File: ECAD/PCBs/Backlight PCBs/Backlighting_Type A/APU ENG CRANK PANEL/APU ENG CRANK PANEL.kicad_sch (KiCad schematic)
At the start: 46 parts, among them J1 Molex 2x02 Mini-Fit Jr., J2 Molex 2x02 Mini-Fit Jr.

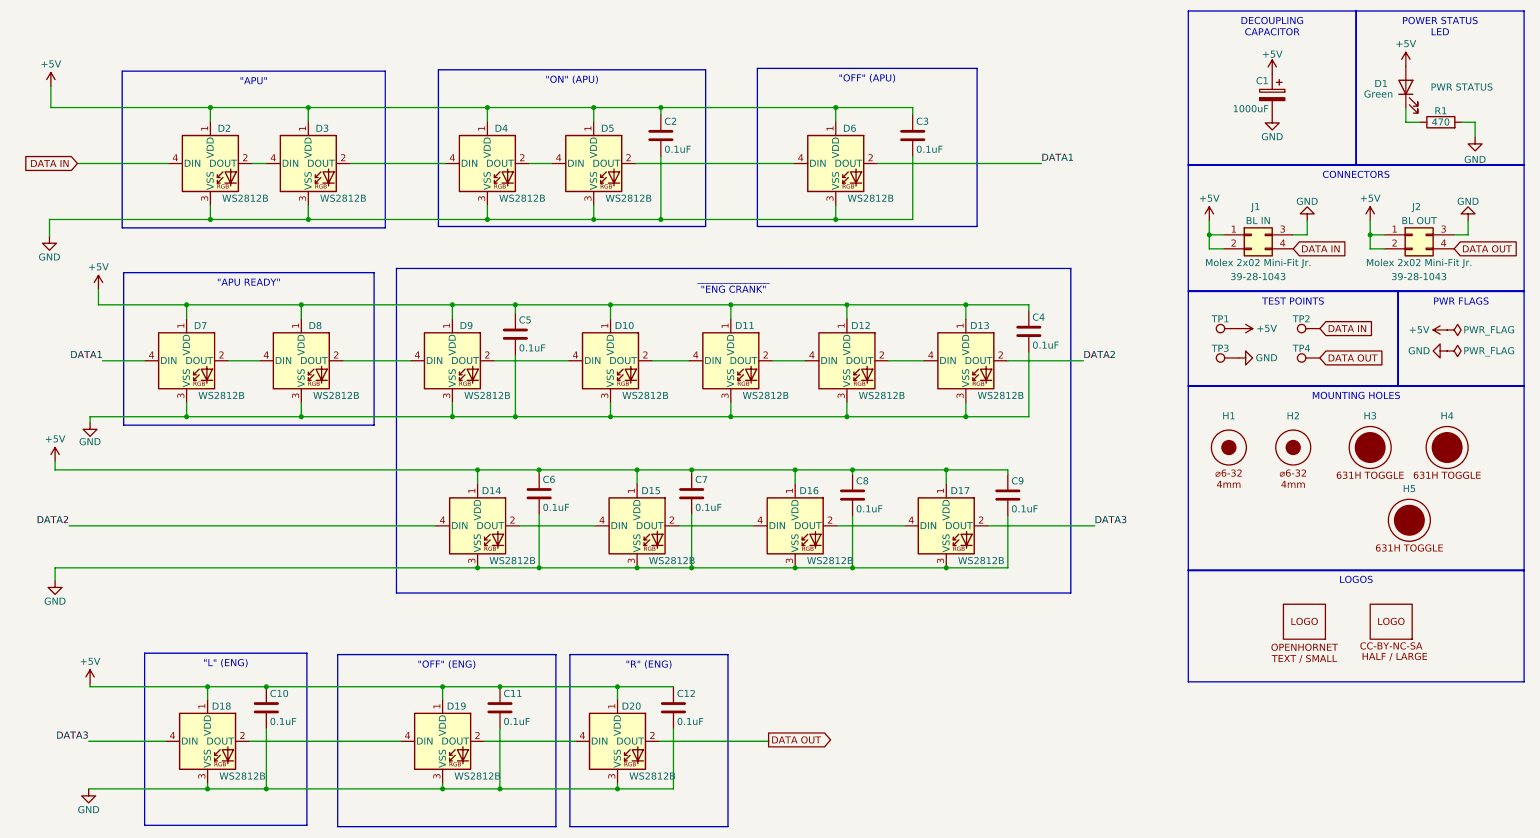
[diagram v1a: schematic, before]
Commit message: Updated schematics:  ANT SEL & APU ENG panels
1:  Updated Schematic/PCB Netlists from default to 5v/GND as required.
2:  Reannotated Test Point references designators.  To prevent confusion, TP1 & 2 will also be Power/Ground respectively; TP3 and TP4 will be Data In/Data Out respectively.
3:  Updated schematic/pcb with symbol/footprint metadata
4:  Fixed "DATA OUT" symbols on TestPoint and J2 connector to show output instead of input.
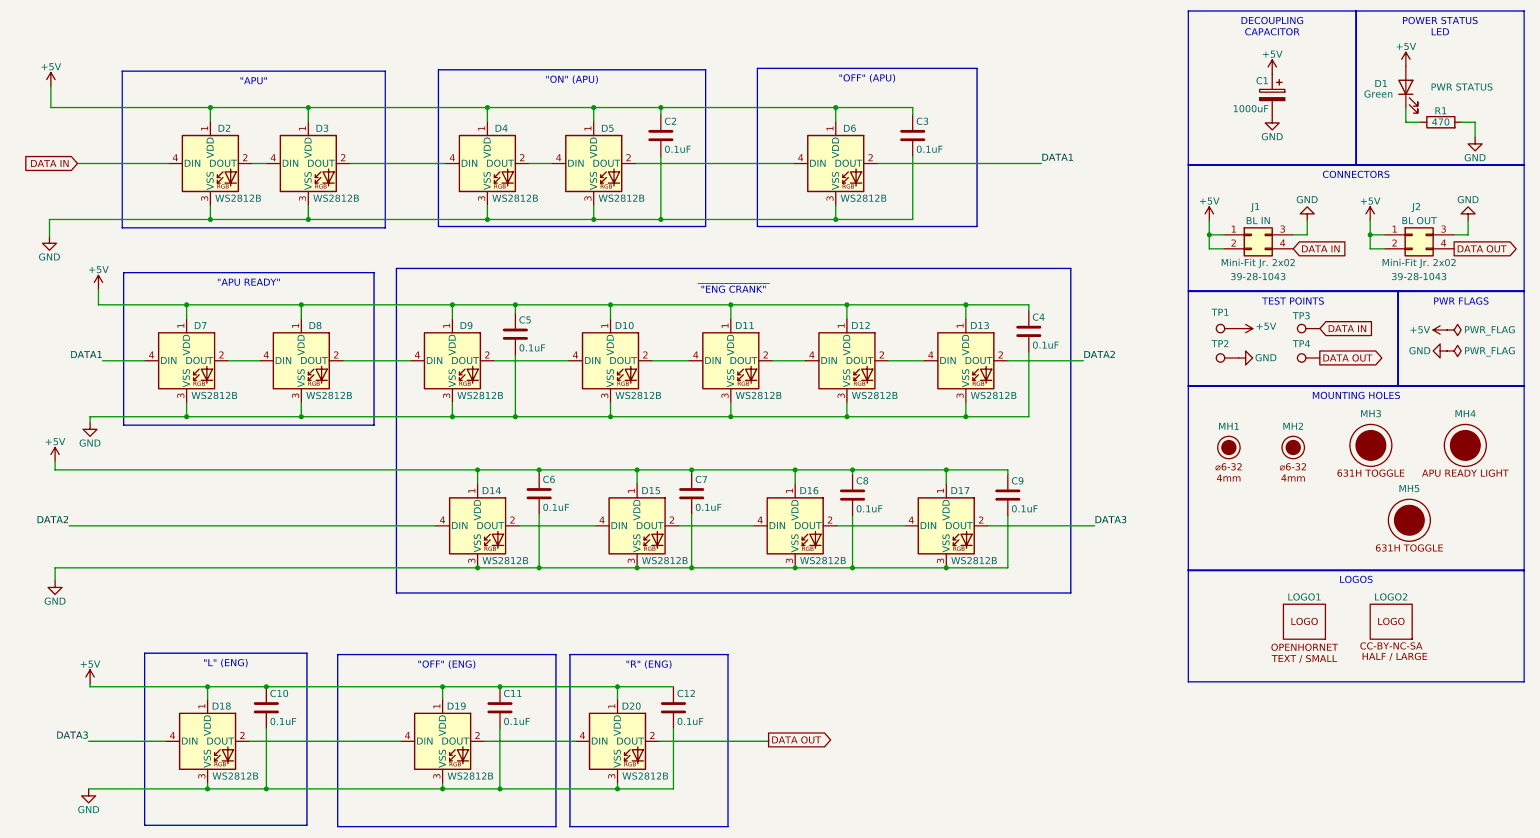
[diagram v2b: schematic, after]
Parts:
- D10, D11, D12, D13, D14, D15, D16, D17, D18, D19, D2, D20, D3, D4, D5, D6, D7, D8, D9: value RGB -> WS2812B
- J1, J2: value Molex 2x02 Mini-Fit Jr. -> Mini-Fit Jr. 2x02; symbol OH_Symbols:Molex_2x02_Mini-Fit_Jr. -> OH_Symbols:Molex_Mini-Fit_Jr._2x02
- LOGO2, TP1, TP4: now left out of the parts list
- MH1: renamed from H1; now left out of the parts list
- MH2: renamed from H2; now left out of the parts list
- MH3: renamed from H3; value MountingHole_631H_Toggle -> Switch_631H; footprint OH_Footprints:631H_Toggle_13mm_x_13mm -> OH_Footprints:631HX_Toggle_13mm_x_13mm; Manufacturer PN (none) -> 631H; now left out of the parts list
- MH4: renamed from H4; value MountingHole_631H_Toggle -> APU READY LIGHT; footprint OH_Footprints:631H_Toggle_13mm_x_13mm -> OH_Footprints:631HX_Toggle_13mm_x_13mm; now left out of the parts list
- MH5: renamed from H5; value MountingHole_631H_Toggle -> Switch_631H; footprint OH_Footprints:631H_Toggle_13mm_x_13mm -> OH_Footprints:631HX_Toggle_13mm_x_13mm; Manufacturer PN (none) -> 631H; now left out of the parts list
- TP2: renamed from TP3; now left out of the parts list
- TP3: renamed from TP2; now left out of the parts list
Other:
- moved on the sheet: MH4, TP1, TP2, TP3, TP4
